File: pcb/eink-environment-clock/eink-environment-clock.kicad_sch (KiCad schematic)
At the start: 23 parts, among them J1 J1_PWR, J2 J2_EPD, U1 U1_ESP32C3, U2 U2_BME280, U3 RTC_DS3231, U4 U4_MH-Z19B

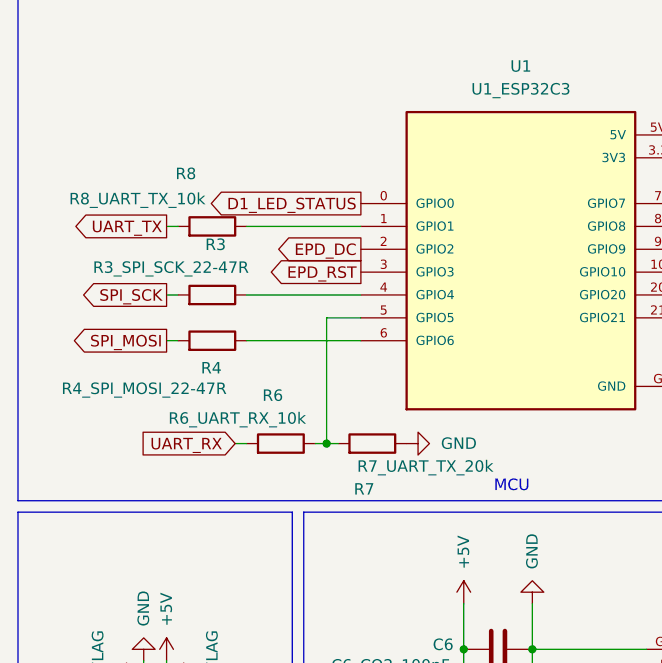
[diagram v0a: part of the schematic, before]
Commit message: feat(pcb): Add images and update R8
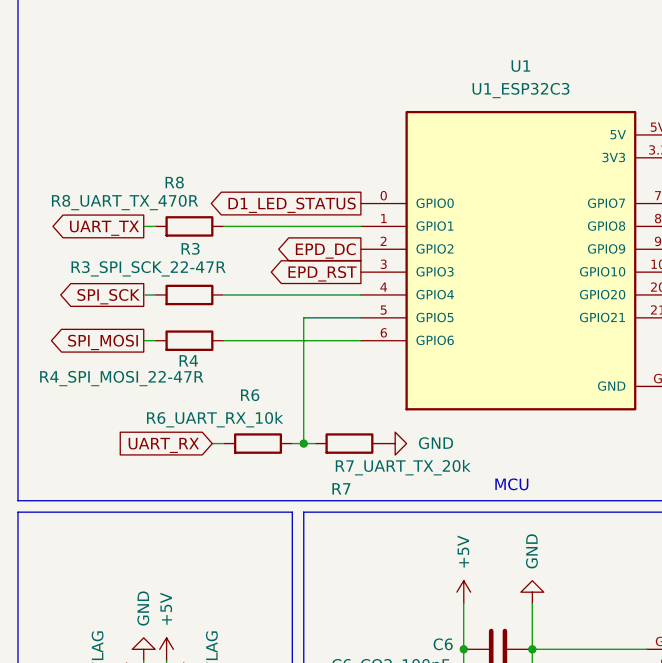
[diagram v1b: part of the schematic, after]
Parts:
- R8: value R8_UART_TX_10k -> R8_UART_TX_470R
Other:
- moved on the sheet: R3, R4, R6, R7, R8
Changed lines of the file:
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@@
 	)
 	(junction
-		(at 55.88 67.31)
+		(at 53.34 67.31)
 		(diameter 0)
 		(color 0 0 0 0)
@@
 	(wire
 		(pts
-			(xy 46.99 55.88) (xy 59.69 55.88)
+			(xy 44.45 55.88) (xy 59.69 55.88)
 		)
 		(stroke
@@
 	(wire
 		(pts
-			(xy 59.69 53.34) (xy 55.88 53.34)
+			(xy 59.69 53.34) (xy 53.34 53.34)
 		)
 		(stroke
@@
 	(wire
 		(pts
-			(xy 38.1 55.88) (xy 39.37 55.88)
+			(xy 35.56 55.88) (xy 36.83 55.88)
 		)
 		(stroke
@@
 	(wire
 		(pts
-			(xy 46.99 43.18) (xy 59.69 43.18)
+			(xy 44.45 43.18) (xy 59.69 43.18)
 		)
 		(stroke
@@
 	(wire
 		(pts
-			(xy 45.72 67.31) (xy 46.99 67.31)
+			(xy 43.18 67.31) (xy 44.45 67.31)
 		)
 		(stroke
@@
 	(wire
 		(pts
-			(xy 55.88 53.34) (xy 55.88 67.31)
+			(xy 53.34 53.34) (xy 53.34 67.31)
 		)
 		(stroke
@@
 	(wire
 		(pts
-			(xy 54.61 67.31) (xy 55.88 67.31)
+			(xy 52.07 67.31) (xy 53.34 67.31)
 		)
 		(stroke
@@
 	(wire
 		(pts
-			(xy 38.1 50.8) (xy 39.37 50.8)
+			(xy 35.56 50.8) (xy 36.83 50.8)
 		)
 		(stroke
@@
 	(wire
 		(pts
-			(xy 46.99 50.8) (xy 59.69 50.8)
+			(xy 44.45 50.8) (xy 59.69 50.8)
 		)
 		(stroke
@@
 	(wire
 		(pts
-			(xy 55.88 67.31) (xy 57.15 67.31)
+			(xy 53.34 67.31) (xy 54.61 67.31)
 		)
 		(stroke
@@
 	(wire
 		(pts
-			(xy 38.1 43.18) (xy 39.37 43.18)
+			(xy 35.56 43.18) (xy 36.83 43.18)
 		)
 		(stroke
@@
 	(global_label "UART_RX"
 		(shape input)
-		(at 45.72 67.31 180)
+		(at 43.18 67.31 180)
 		(fields_autoplaced yes)
 		(effects
@@
 		)
 		(property "Intersheetrefs" "${INTERSHEET_REFS}"
-			(at 34.631 67.31 0)
+			(at 32.091 67.31 0)
 			(effects
 				(font
@@
 	(global_label "UART_TX"
 		(shape output)
-		(at 38.1 43.18 180)
+		(at 35.56 43.18 180)
 		(fields_autoplaced yes)
 		(effects
@@
 		)
 		(property "Intersheetrefs" "${INTERSHEET_REFS}"
-			(at 27.3134 43.18 0)
+			(at 24.7734 43.18 0)
 			(effects
 				(font
@@
 	(global_label "SPI_SCK"
 		(shape output)
-		(at 38.1 50.8 180)
+		(at 35.56 50.8 180)
 		(fields_autoplaced yes)
 		(effects
@@
 		)
 		(property "Intersheetrefs" "${INTERSHEET_REFS}"
-			(at 27.3134 50.8 0)
+			(at 24.7734 50.8 0)
 			(effects
 				(font
@@
 	(global_label "SPI_MOSI"
 		(shape output)
-		(at 38.1 55.88 180)
+		(at 35.56 55.88 180)
 		(fields_autoplaced yes)
 		(effects
@@
 		)
 		(property "Intersheetrefs" "${INTERSHEET_REFS}"
-			(at 26.4667 55.88 0)
+			(at 23.9267 55.88 0)
 			(effects
 				(font
@@
 	(symbol
 		(lib_id "Device:R")
-		(at 60.96 67.31 270)
+		(at 58.42 67.31 270)
 		(mirror x)
 		(unit 1)
@@
 		(dnp no)
 		(property "Reference" "R7"
-			(at 61.214 72.39 90)
+			(at 58.674 72.39 90)
 			(effects
 				(font
@@
 		)
 		(property "Value" "R7_UART_TX_20k"
-			(at 74.422 69.85 90)
+			(at 71.882 69.85 90)
 			(effects
 				(font
@@
 		)
 		(property "Footprint" "Resistor_THT:R_Axial_DIN0207_L6.3mm_D2.5mm_P7.62mm_Horizontal"
-			(at 60.96 69.088 90)
+			(at 58.42 69.088 90)
 			(effects
 				(font
@@
 		)
 		(property "Datasheet" "~"
-			(at 60.96 67.31 0)
+			(at 58.42 67.31 0)
 			(effects
 				(font
@@
 		)
 		(property "Description" "Resistor"
-			(at 60.96 67.31 0)
+			(at 58.42 67.31 0)
 			(effects
 				(font
@@
 	(symbol
 		(lib_id "Device:R")
-		(at 50.8 67.31 270)
+		(at 48.26 67.31 270)
 		(mirror x)
 		(unit 1)
@@
 		(dnp no)
 		(property "Reference" "R6"
-			(at 51.054 61.976 90)
+			(at 48.514 61.976 90)
 			(effects
 				(font
@@
 		)
 		(property "Value" "R6_UART_RX_10k"
-			(at 53.594 64.516 90)
+			(at 51.054 64.516 90)
 			(effects
 				(font
@@
 		)
 		(property "Footprint" "Resistor_THT:R_Axial_DIN0207_L6.3mm_D2.5mm_P7.62mm_Horizontal"
-			(at 50.8 69.088 90)
+			(at 48.26 69.088 90)
 			(effects
 				(font
@@
 		)
 		(property "Datasheet" "~"
-			(at 50.8 67.31 0)
+			(at 48.26 67.31 0)
 			(effects
 				(font
@@
 		)
 		(property "Description" "Resistor"
-			(at 50.8 67.31 0)
+			(at 48.26 67.31 0)
 			(effects
 				(font
@@
 	(symbol
 		(lib_id "power:GND")
-		(at 64.77 67.31 90)
+		(at 62.23 67.31 90)
 		(unit 1)
 		(exclude_from_sim no)
@@
 		(fields_autoplaced yes)
 		(property "Reference" "#PWR010"
-			(at 71.12 67.31 0)
+			(at 68.58 67.31 0)
 			(effects
 				(font
@@
 		)
 		(property "Value" "GND"
-			(at 68.58 67.3099 90)
+			(at 66.04 67.3099 90)
 			(effects
 				(font
@@
 		)
 		(property "Footprint" ""
-			(at 64.77 67.31 0)
+			(at 62.23 67.31 0)
 			(effects
 				(font
@@
 		)
 		(property "Datasheet" ""
-			(at 64.77 67.31 0)
+			(at 62.23 67.31 0)
 			(effects
 				(font
@@
 		)
 		(property "Description" "Power symbol creates a global label with name \"GND\" , ground"
-			(at 64.77 67.31 0)
+			(at 62.23 67.31 0)
 			(effects
 				(font
@@
 	(symbol
 		(lib_id "Device:R")
-		(at 43.18 43.18 270)
+		(at 40.64 43.18 270)
 		(mirror x)
 		(unit 1)
@@
 		(dnp no)
 		(property "Reference" "R8"
-			(at 41.402 37.338 90)
+			(at 40.132 38.354 90)
 			(effects
 				(font
@@
 			)
 		)
-		(property "Value" "R8_UART_TX_10k"
-			(at 42.418 40.132 90)
+		(property "Value" "R8_UART_TX_470R"
+			(at 41.656 40.386 90)
 			(effects
 				(font
@@
 		)
 		(property "Footprint" "Resistor_THT:R_Axial_DIN0207_L6.3mm_D2.5mm_P7.62mm_Horizontal"
-			(at 43.18 44.958 90)
+			(at 40.64 44.958 90)
 			(effects
 				(font
@@
 		)
 		(property "Datasheet" "~"
-			(at 43.18 43.18 0)
+			(at 40.64 43.18 0)
 			(effects
 				(font
@@
 		)
 		(property "Description" "Resistor"
-			(at 43.18 43.18 0)
+			(at 40.64 43.18 0)
 			(effects
 				(font
@@
 	(symbol
 		(lib_id "Device:R")
-		(at 43.18 50.8 270)
+		(at 40.64 50.8 270)
 		(mirror x)
 		(unit 1)
@@
 		(dnp no)
 		(property "Reference" "R3"
-			(at 44.704 45.212 90)
+			(at 41.91 45.72 90)
 			(effects
 				(font
@@
 		)
 		(property "Value" "R3_SPI_SCK_22-47R"
-			(at 47.244 47.752 90)
+			(at 44.704 47.752 90)
 			(effects
 				(font
@@
 		)
 		(property "Footprint" "Resistor_THT:R_Axial_DIN0207_L6.3mm_D2.5mm_P7.62mm_Horizontal"
-			(at 43.18 52.578 90)
+			(at 40.64 52.578 90)
 			(effects
 				(font
@@
 		)
 		(property "Datasheet" "~"
-			(at 43.18 50.8 0)
+			(at 40.64 50.8 0)
 			(effects
 				(font
@@
 		)
 		(property "Description" "Resistor"
-			(at 43.18 50.8 0)
+			(at 40.64 50.8 0)
 			(effects
 				(font
@@
 	(symbol
 		(lib_id "Device:R")
-		(at 43.18 55.88 270)
+		(at 40.64 55.88 270)
 		(mirror x)
 		(unit 1)
@@
 		(dnp no)
 		(property "Reference" "R4"
-			(at 41.91 58.928 90)
+			(at 39.37 58.166 90)
 			(effects
 				(font
@@
 		)
 		(property "Value" "R4_SPI_MOSI_22-47R"
-			(at 26.416 61.214 90)
+			(at 23.876 59.944 90)
 			(effects
 				(font
@@
 		)
 		(property "Footprint" "Resistor_THT:R_Axial_DIN0207_L6.3mm_D2.5mm_P7.62mm_Horizontal"
-			(at 43.18 57.658 90)
+			(at 40.64 57.658 90)
 			(effects
 				(font
@@
 		)
 		(property "Datasheet" "~"
-			(at 43.18 55.88 0)
+			(at 40.64 55.88 0)
 			(effects
 				(font
@@
 		)
 		(property "Description" "Resistor"
-			(at 43.18 55.88 0)
+			(at 40.64 55.88 0)
 			(effects
 				(font
